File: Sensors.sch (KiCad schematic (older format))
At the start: 27 parts, among them P4 CONN_01X04, Q1 PMosfetGen, Q2 PMosfetGen, Q4 PMosfetGen, U1 PIR, U2 MCP6004

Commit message: Fix Boot0 pin and add prices per component
Signed-off-by: Philip Luyckx <philip.luyckx@gmail.com>
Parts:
- C10, C11, C13, C14, C7: Price (none) -> 0.02
- C12: value C -> 100nF; Price (none) -> 0.02
- D2: Price (none) -> 0.34
- Q1, Q2, Q4: value PMosfetGen -> AO3401; Price (none) -> 0.06
- R10, R12, R13, R14, R15, R16, R17, R3, R4, R5, R6, R7, R9: Price (none) -> 0.01
- U1: Price (none) -> 1.31
- U2: Price (none) -> 0.25
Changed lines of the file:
@@
 F 2 "CustomModules:PIR" H 4900 2550 60  0001 C CNN
 F 3 "" H 4900 2550 60  0000 C CNN
+F 4 "1.31" H 4900 2550 60  0001 C CNN "Price"
 	1    4900 2550
 	-1   0    0    -1
@@
 P 6150 1450
 F 0 "Q2" H 6470 1500 60  0000 C CNN
-F 1 "PMosfetGen" H 6470 1400 60  0000 C CNN
+F 1 "AO3401" H 6470 1400 60  0000 C CNN
 F 2 "CustomSmd:SOT23" H 6100 1590 60  0001 C CNN
 F 3 "" H 6100 1590 60  0000 C CNN
+F 4 "0.06" H 6150 1450 60  0001 C CNN "Price"
 	1    6150 1450
 	1    0    0    1
@@
 F 2 "Resistors_SMD:R_0603" V 5780 1200 30  0001 C CNN
 F 3 "" H 5850 1200 30  0000 C CNN
+F 4 "0.01" V 5850 1200 60  0001 C CNN "Price"
 	1    5850 1200
 	1    0    0    -1
@@
 P 2000 1350
 F 0 "Q4" H 2320 1400 60  0000 C CNN
-F 1 "PMosfetGen" H 2320 1300 60  0000 C CNN
+F 1 "AO3401" H 2320 1300 60  0000 C CNN
 F 2 "CustomSmd:SOT23" H 1950 1490 60  0001 C CNN
 F 3 "" H 1950 1490 60  0000 C CNN
+F 4 "0.06" H 2000 1350 60  0001 C CNN "Price"
 	1    2000 1350
 	1    0    0    1
@@
 F 2 "Resistors_SMD:R_0603" V 1630 1100 30  0001 C CNN
 F 3 "" H 1700 1100 30  0000 C CNN
+F 4 "0.01" V 1700 1100 60  0001 C CNN "Price"
 	1    1700 1100
 	1    0    0    -1
@@
 P 1900 4800
 F 0 "Q1" H 2220 4850 60  0000 C CNN
-F 1 "PMosfetGen" H 2220 4750 60  0000 C CNN
+F 1 "AO3401" H 2220 4750 60  0000 C CNN
 F 2 "CustomSmd:SOT23" H 1850 4940 60  0001 C CNN
 F 3 "" H 1850 4940 60  0000 C CNN
+F 4 "0.06" H 1900 4800 60  0001 C CNN "Price"
 	1    1900 4800
 	1    0    0    1
@@
 F 2 "Resistors_SMD:R_0603" V 1530 4550 30  0001 C CNN
 F 3 "" H 1600 4550 30  0000 C CNN
+F 4 "0.01" V 1600 4550 60  0001 C CNN "Price"
 	1    1600 4550
 	1    0    0    -1
@@
 F 2 "Resistors_SMD:R_0603" V 5330 2900 30  0001 C CNN
 F 3 "" H 5400 2900 30  0000 C CNN
+F 4 "0.01" V 5400 2900 60  0001 C CNN "Price"
 	1    5400 2900
 	-1   0    0    -1
@@
 F 2 "Resistors_SMD:R_0805" H 6188 1850 30  0001 C CNN
 F 3 "" H 6150 2000 60  0000 C CNN
+F 4 "0.02" H 6150 2000 60  0001 C CNN "Price"
 	1    6150 2000
 	1    0    0    -1
@@
 F 2 "Resistors_SMD:R_0603" V 5380 4250 50  0001 C CNN
 F 3 "" H 5450 4250 50  0000 C CNN
+F 4 "0.01" V 5450 4250 60  0001 C CNN "Price"
 	1    5450 4250
 	0    1    1    0
@@
 P 6750 2850
 F 0 "C12" H 6775 2950 50  0000 L CNN
-F 1 "C" H 6775 2750 50  0000 L CNN
+F 1 "100nF" H 6775 2750 50  0000 L CNN
 F 2 "Resistors_SMD:R_0805" H 6788 2700 50  0001 C CNN
 F 3 "" H 6750 2850 50  0000 C CNN
+F 4 "0.02" H 6750 2850 60  0001 C CNN "Price"
 	1    6750 2850
 	1    0    0    -1
@@
 F 2 "Resistors_SMD:R_0603" V 7180 2900 50  0001 C CNN
 F 3 "" H 7250 2900 50  0000 C CNN
+F 4 "0.01" V 7250 2900 60  0001 C CNN "Price"
 	1    7250 2900
 	1    0    0    -1
@@
 F 2 "Resistors_SMD:R_0603" V 7180 3300 50  0001 C CNN
 F 3 "" H 7250 3300 50  0000 C CNN
+F 4 "0.01" V 7250 3300 60  0001 C CNN "Price"
 	1    7250 3300
 	1    0    0    -1
@@
 F 2 "Resistors_SMD:R_0805" H 5788 4100 50  0001 C CNN
 F 3 "" H 5750 4250 50  0000 C CNN
+F 4 "0.02" H 5750 4250 60  0001 C CNN "Price"
 	1    5750 4250
 	0    -1   -1   0
@@
 F 2 "Resistors_SMD:R_0603" V 6180 5100 50  0001 C CNN
 F 3 "" H 6250 5100 50  0000 C CNN
+F 4 "0.01" V 6250 5100 60  0001 C CNN "Price"
 	1    6250 5100
 	0    1    1    0
@@
 F 2 "Resistors_SMD:R_0805" H 6288 4600 50  0001 C CNN
 F 3 "" H 6250 4750 50  0000 C CNN
+F 4 "0.02" H 6250 4750 60  0001 C CNN "Price"
 	1    6250 4750
 	0    1    1    0
@@
 F 2 "Resistors_SMD:R_0603" V 6980 4150 50  0001 C CNN
 F 3 "" H 7050 4150 50  0000 C CNN
+F 4 "0.01" V 7050 4150 60  0001 C CNN "Price"
 	1    7050 4150
 	0    1    1    0
@@
 F 2 "Resistors_SMD:R_0805" H 7388 4000 50  0001 C CNN
 F 3 "" H 7350 4150 50  0000 C CNN
+F 4 "0.02" H 7350 4150 60  0001 C CNN "Price"
 	1    7350 4150
 	0    -1   -1   0
@@
 F 2 "Resistors_SMD:R_0603" V 7780 5000 50  0001 C CNN
 F 3 "" H 7850 5000 50  0000 C CNN
+F 4 "0.01" V 7850 5000 60  0001 C CNN "Price"
 	1    7850 5000
 	0    1    1    0
@@
 F 2 "Resistors_SMD:R_0805" H 7888 4500 50  0001 C CNN
 F 3 "" H 7850 4650 50  0000 C CNN
+F 4 "0.02" H 7850 4650 60  0001 C CNN "Price"
 	1    7850 4650
 	0    1    1    0
@@
 F 2 "Resistors_SMD:R_0603" V 6730 4550 50  0001 C CNN
 F 3 "" H 6800 4550 50  0000 C CNN
+F 4 "0.01" V 6800 4550 60  0001 C CNN "Price"
 	1    6800 4550
 	1    0    0    -1
@@
 F 2 "Resistors_SMD:R_0603" V 8430 4450 50  0001 C CNN
 F 3 "" H 8500 4450 50  0000 C CNN
+F 4 "0.01" V 8500 4450 60  0001 C CNN "Price"
 	1    8500 4450
 	1    0    0    -1
@@
 F 2 "CustomModules:PD638C" H 2000 2550 60  0001 C CNN
 F 3 "" H 2000 2550 60  0000 C CNN
+F 4 "0.34" H 2000 2550 60  0001 C CNN "Price"
 	1    2000 2550
 	1    0    0    -1
@@
 F 2 "CustomSmd:SOIC-14" H 2750 2600 50  0001 C CNN
 F 3 "" H 2850 2700 50  0000 C CNN
+F 4 "0.25" H 2800 2500 60  0001 C CNN "Price"
 	4    2800 2500
 	1    0    0    -1
@@
 F 2 "Resistors_SMD:R_0603" V 1630 5300 50  0001 C CNN
 F 3 "" H 1700 5300 50  0000 C CNN
+F 4 "0.01" V 1700 5300 60  0001 C CNN "Price"
 	1    1700 5300
 	1    0    0    -1

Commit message: Update schematics for V3:
 * Change DHT22 to HTU21D
 * Change schematic for MCP6044
 * Correct unused opamp + power supply
 * Reassign some cpu pins (for HTU21D)
 * Add LDO power supply for 1.8V
 * Update STM32CubeMx project
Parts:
- removed P4: CONN_01X04, Socket_Strips:Socket_Strip_Angled_1x04, symbol CONN_01X04
- removed Q1, Q4: AO3401, CustomSmd:SOT23, symbol PMosfetGen
- removed R10, R16: 10k, Resistors_SMD:R_0603, symbol R
- removed R17: 1k, Resistors_SMD:R_0603, symbol R
- removed R4, R7: 47.5k, Resistors_SMD:R_0603, symbol R
- removed U2: MCP6004, CustomSmd:SOIC-14, symbol MCP6004
- added C10, C9: 100nF, symbol C
- added C8: 1uF, symbol C
- added U1: MCP60x4, symbol MCP60x4
- added U2: HTU21D, symbol HTU21D
- R11: renamed from R13; value 100k -> 1M
- R12: renamed from R14; value 100k -> 1M
- renumbered C10 to C11, C7 to C12, C11 to C13, C12 to C14, C13 to C15, C14 to C16, Q2 to Q1, R12 to R10, R15 to R13, R8 to R5, R3 to R6, R6 to R7, R5 to R8, U1 to U3
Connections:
- net labels added: +1V8, +BATT, HTU21_SCK, HTU21_SDA
- net labels removed: DHT22_Enable, OpampEnable, Opamp_V+, Temp_1Wire, VCC
- wire segments 59 -> 58
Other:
- note added: "Opamp supply"
- note added: "Reached 0,5mA\nin short circuit\nVCC is 1.8V"
- note added: "Temperature & Humidity sensor"
- note added: "Unused opamp"
- note removed: "DHT22/AM2303"
- note removed: "Reached 0,5mA\nin short circuit\nVCC can go down\nto 2V"
- note removed: "Todo:\n * Check if opamp truly clips at vcc and gnd"
- moved on the sheet: D2, R5

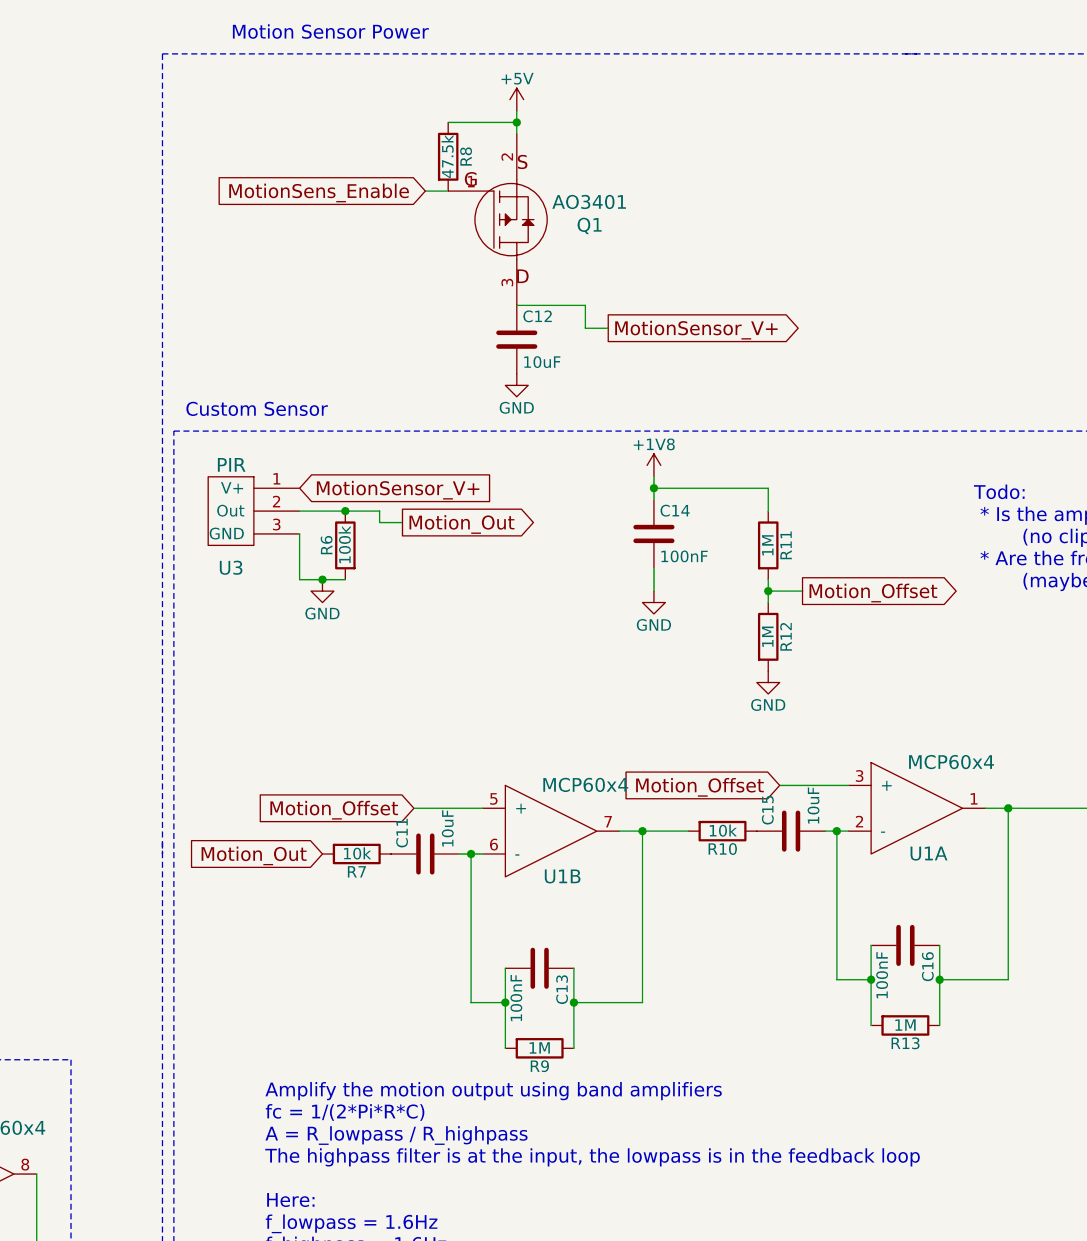
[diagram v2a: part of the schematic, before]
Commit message: Updates for V3:
 * Remove unnecessary power supply enable MOSFETs
 * Optimize pin configuration

Signed-off-by: pluyckx <philip.luyckx@gmail.com>
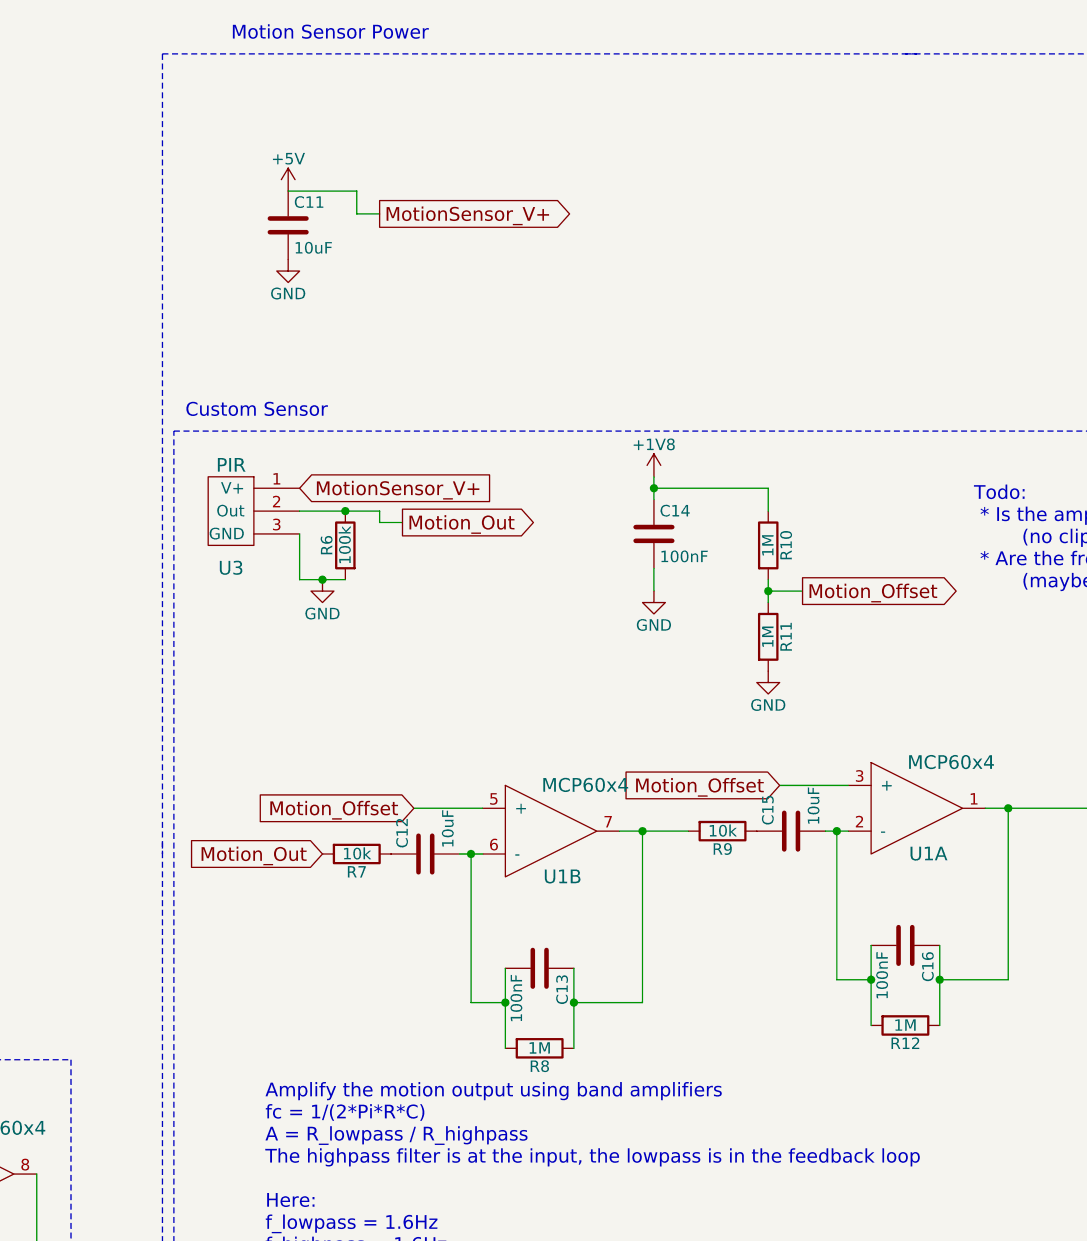
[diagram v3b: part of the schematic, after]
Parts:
- removed Q1: AO3401, CustomSmd:SOT23, symbol PMosfetGen
- removed R8: 47.5k, Resistors_SMD:R_0603, symbol R
- renumbered C12 to C11, C11 to C12, R11 to R10, R12 to R11, R13 to R12, R9 to R8, R10 to R9
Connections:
- net MotionSensor_V+ is gone; now on net +5V: C11.1, U3.1 (V+)
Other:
- moved on the sheet: C11
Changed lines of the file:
@@
 $EndDescr
 $Comp
-L +5V #PWR26
+L +5V #PWR019
 U 1 1 56622EB6
-P 6150 1000
-F 0 "#PWR26" H 6150 850 50  0001 C CNN
-F 1 "+5V" H 6150 1140 50  0000 C CNN
-F 2 "" H 6150 1000 60  0000 C CNN
-F 3 "" H 6150 1000 60  0000 C CNN
-	1    6150 1000
-	1    0    0    -1
-$EndComp
-$Comp
-L GND #PWR25
+P 5150 1350
+F 0 "#PWR019" H 5150 1200 50  0001 C CNN
+F 1 "+5V" H 5150 1490 50  0000 C CNN
+F 2 "" H 5150 1350 60  0000 C CNN
+F 3 "" H 5150 1350 60  0000 C CNN
+	1    5150 1350
+	1    0    0    -1
+$EndComp
+$Comp
+L GND #PWR020
 U 1 1 56622ECA
 P 5300 3050
-F 0 "#PWR25" H 5300 2800 50  0001 C CNN
+F 0 "#PWR020" H 5300 2800 50  0001 C CNN
 F 1 "GND" H 5300 2900 50  0000 C CNN
 F 2 "" H 5300 3050 60  0000 C CNN
@@
 	-1   0    0    -1
 $EndComp
-$Comp
-L PMosfetGen Q1
-U 1 1 56623098
-P 6150 1450
-F 0 "Q1" H 6470 1500 60  0000 C CNN
-F 1 "AO3401" H 6470 1400 60  0000 C CNN
-F 2 "CustomSmd:SOT23" H 6100 1590 60  0001 C CNN
-F 3 "" H 6100 1590 60  0000 C CNN
-F 4 "0.06" H 6150 1450 60  0001 C CNN "Price"
-	1    6150 1450
-	1    0    0    1
-$EndComp
-$Comp
-L R R8
-U 1 1 566230C3
-P 5850 1200
-F 0 "R8" V 5930 1200 50  0000 C CNN
-F 1 "47.5k" V 5850 1200 50  0000 C CNN
-F 2 "Resistors_SMD:R_0603" V 5780 1200 30  0001 C CNN
-F 3 "" H 5850 1200 30  0000 C CNN
-F 4 "0.01" V 5850 1200 60  0001 C CNN "Price"
-	1    5850 1200
-	1    0    0    -1
-$EndComp
-Text GLabel 5750 1350 0    60   Input ~ 0
-MotionSens_Enable
 Text GLabel 5200 2650 2    60   Input ~ 0
 MotionSensor_V+
-Text GLabel 6550 1950 2    60   Output ~ 0
+Text GLabel 5550 1450 2    60   Output ~ 0
 MotionSensor_V+
 Text Notes 4900 700  0    60   ~ 0
@@
 Text Notes 750  700  0    60   ~ 0
 Light Sensor
-Wire Wire Line
-	6150 1000 6150 1100
 Wire Notes Line
 	3650 800  650  800
-Wire Wire Line
-	5850 1050 6150 1050
-Connection ~ 6150 1050
-Wire Wire Line
-	5750 1350 5850 1350
 $Comp
 L R R6
@@
 Connection ~ 5300 3050
 $Comp
-L C C12
+L C C11
 U 1 1 56637A5D
-P 6150 2000
-F 0 "C12" H 6175 2100 50  0000 L CNN
-F 1 "10uF" H 6175 1900 50  0000 L CNN
-F 2 "Resistors_SMD:R_0805" H 6188 1850 30  0001 C CNN
-F 3 "" H 6150 2000 60  0000 C CNN
-F 4 "0.02" H 6150 2000 60  0001 C CNN "Price"
-	1    6150 2000
-	1    0    0    -1
-$EndComp
-$Comp
-L GND #PWR27
+P 5150 1500
+F 0 "C11" H 5175 1600 50  0000 L CNN
+F 1 "10uF" H 5175 1400 50  0000 L CNN
+F 2 "Resistors_SMD:R_0805" H 5188 1350 30  0001 C CNN
+F 3 "" H 5150 1500 60  0000 C CNN
+F 4 "0.02" H 5150 1500 60  0001 C CNN "Price"
+	1    5150 1500
+	1    0    0    -1
+$EndComp
+$Comp
+L GND #PWR021
 U 1 1 56637ADC
-P 6150 2150
-F 0 "#PWR27" H 6150 1900 50  0001 C CNN
-F 1 "GND" H 6150 2000 50  0000 C CNN
-F 2 "" H 6150 2150 60  0000 C CNN
-F 3 "" H 6150 2150 60  0000 C CNN
-	1    6150 2150
-	1    0    0    -1
-$EndComp
-Wire Wire Line
-	6150 1850 6450 1850
-Wire Wire Line
-	6450 1850 6450 1950
-Wire Wire Line
-	6450 1950 6550 1950
-$Comp
-L GND #PWR23
+P 5150 1650
+F 0 "#PWR021" H 5150 1400 50  0001 C CNN
+F 1 "GND" H 5150 1500 50  0000 C CNN
+F 2 "" H 5150 1650 60  0000 C CNN
+F 3 "" H 5150 1650 60  0000 C CNN
+	1    5150 1650
+	1    0    0    -1
+$EndComp
+Wire Wire Line
+	5150 1350 5450 1350
+Wire Wire Line
+	5450 1350 5450 1450
+Wire Wire Line
+	5450 1450 5550 1450
+$Comp
+L GND #PWR022
 U 1 1 5662F07B
 P 1900 1900
-F 0 "#PWR23" H 1900 1650 50  0001 C CNN
+F 0 "#PWR022" H 1900 1650 50  0001 C CNN
 F 1 "GND" H 1900 1750 50  0000 C CNN
 F 2 "" H 1900 1900 60  0000 C CNN
@@
 $EndComp
 $Comp
-L GND #PWR29
+L GND #PWR023
 U 1 1 56A50277
 P 6750 3100
-F 0 "#PWR29" H 6750 2850 50  0001 C CNN
+F 0 "#PWR023" H 6750 2850 50  0001 C CNN
 F 1 "GND" H 6750 2950 50  0000 C CNN
 F 2 "" H 6750 3100 50  0000 C CNN
@@
 Connection ~ 6750 2650
 $Comp
-L R R11
+L R R10
 U 1 1 56A503DD
 P 7250 2900
-F 0 "R11" V 7330 2900 50  0000 C CNN
+F 0 "R10" V 7330 2900 50  0000 C CNN
 F 1 "1M" V 7250 2900 50  0000 C CNN
 F 2 "Resistors_SMD:R_0603" V 7180 2900 50  0001 C CNN
@@
 $EndComp
 $Comp
-L R R12
+L R R11
 U 1 1 56A5048C
 P 7250 3300
-F 0 "R12" V 7330 3300 50  0000 C CNN
+F 0 "R11" V 7330 3300 50  0000 C CNN
 F 1 "1M" V 7250 3300 50  0000 C CNN
 F 2 "Resistors_SMD:R_0603" V 7180 3300 50  0001 C CNN
@@
 $EndComp
 $Comp
-L GND #PWR30
+L GND #PWR024
 U 1 1 56A504D9
 P 7250 3450
-F 0 "#PWR30" H 7250 3200 50  0001 C CNN
+F 0 "#PWR024" H 7250 3200 50  0001 C CNN
 F 1 "GND" H 7250 3300 50  0000 C CNN
 F 2 "" H 7250 3450 50  0000 C CNN
@@
 Motion_Offset
 $Comp
-L C C11
+L C C12
 U 1 1 56A5074F
 P 5750 4250
-F 0 "C11" H 5775 4350 50  0000 L CNN
+F 0 "C12" H 5775 4350 50  0000 L CNN
 F 1 "10uF" H 5775 4150 50  0000 L CNN
 F 2 "Resistors_SMD:R_0805" H 5788 4100 50  0001 C CNN
@@
 	5700 4050 6000 4050
 $Comp
-L R R9
+L R R8
 U 1 1 56A50A2A
 P 6250 5100
-F 0 "R9" V 6330 5100 50  0000 C CNN
+F 0 "R8" V 6330 5100 50  0000 C CNN
 F 1 "1M" V 6250 5100 50  0000 C CNN
 F 2 "Resistors_SMD:R_0603" V 6180 5100 50  0001 C CNN
@@
 Connection ~ 6100 4900
 $Comp
-L R R10
+L R R9
 U 1 1 56A5105F
 P 7050 4150
-F 0 "R10" V 7130 4150 50  0000 C CNN
+F 0 "R9" V 7130 4150 50  0000 C CNN
 F 1 "10k" V 7050 4150 50  0000 C CNN
 F 2 "Resistors_SMD:R_0603" V 6980 4150 50  0001 C CNN
@@
 	7300 3950 7600 3950
 $Comp
-L R R13
+L R R12
 U 1 1 56A51075
 P 7850 5000
-F 0 "R13" V 7930 5000 50  0000 C CNN
+F 0 "R12" V 7930 5000 50  0000 C CNN
 F 1 "1M" V 7850 5000 50  0000 C CNN
 F 2 "Resistors_SMD:R_0603" V 7780 5000 50  0001 C CNN
@@
 	1900 1450 1900 1500
 $Comp
-L GND #PWR24
+L GND #PWR025
 U 1 1 56B3CEE7
 P 2250 1250
-F 0 "#PWR24" H 2250 1000 50  0001 C CNN
+F 0 "#PWR025" H 2250 1000 50  0001 C CNN
 F 1 "GND" H 2250 1100 50  0000 C CNN
 F 2 "" H 2250 1250 50  0000 C CNN
@@
 	2250 1250 2400 1250
 $Comp
-L +1V8 #PWR28
+L +1V8 #PWR026
 U 1 1 5752F64E
 P 6750 2600
-F 0 "#PWR28" H 6750 2450 50  0001 C CNN
+F 0 "#PWR026" H 6750 2450 50  0001 C CNN
 F 1 "+1V8" H 6750 2740 50  0000 C CNN
 F 2 "" H 6750 2600 50  0000 C CNN
@@
 	650  2200 650  800
 $Comp
-L +BATT #PWR19
+L +BATT #PWR027
 U 1 1 5753530B
 P 1500 3900
-F 0 "#PWR19" H 1500 3750 50  0001 C CNN
+F 0 "#PWR027" H 1500 3750 50  0001 C CNN
 F 1 "+BATT" H 1500 4040 50  0000 C CNN
 F 2 "" H 1500 3900 50  0000 C CNN
@@
 $EndComp
 $Comp
-L GND #PWR20
+L GND #PWR028
 U 1 1 57535772
 P 1500 4100
-F 0 "#PWR20" H 1500 3850 50  0001 C CNN
+F 0 "#PWR028" H 1500 3850 50  0001 C CNN
 F 1 "GND" H 1500 3950 50  0000 C CNN
 F 2 "" H 1500 4100 50  0000 C CNN
@@
 $EndComp
 $Comp
-L +1V8 #PWR21
+L +1V8 #PWR029
 U 1 1 57539252
 P 1850 5400
-F 0 "#PWR21" H 1850 5250 50  0001 C CNN
+F 0 "#PWR029" H 1850 5250 50  0001 C CNN
 F 1 "+1V8" H 1850 5540 50  0000 C CNN
 F 2 "" H 1850 5400 50  0000 C CNN
@@
 $EndComp
 $Comp
-L GND #PWR22
+L GND #PWR030
 U 1 1 5753929C
 P 1850 6100
-F 0 "#PWR22" H 1850 5850 50  0001 C CNN
+F 0 "#PWR030" H 1850 5850 50  0001 C CNN
 F 1 "GND" H 1850 5950 50  0000 C CNN
 F 2 "" H 1850 6100 50  0000 C CNN
